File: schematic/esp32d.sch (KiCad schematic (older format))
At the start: 47 parts, among them IC1 CP2102N-A01-GQFN28R, J1 USB_B_Micro, J2 Conn_02x08_Odd_Even, J3 Conn_02x08_Odd_Even, J4 Conn_01x02, Q1 SS8050-G, Q2 SS8050-G, Q3 DMG2307L-7, SW1 SW_Push, U1 AMS1117-3.3, U2 ESP32-WROOM-32D, U3 DizzyBITLogo, U4 MCP73831-2-OT, U5 DizzyBIT-Layout

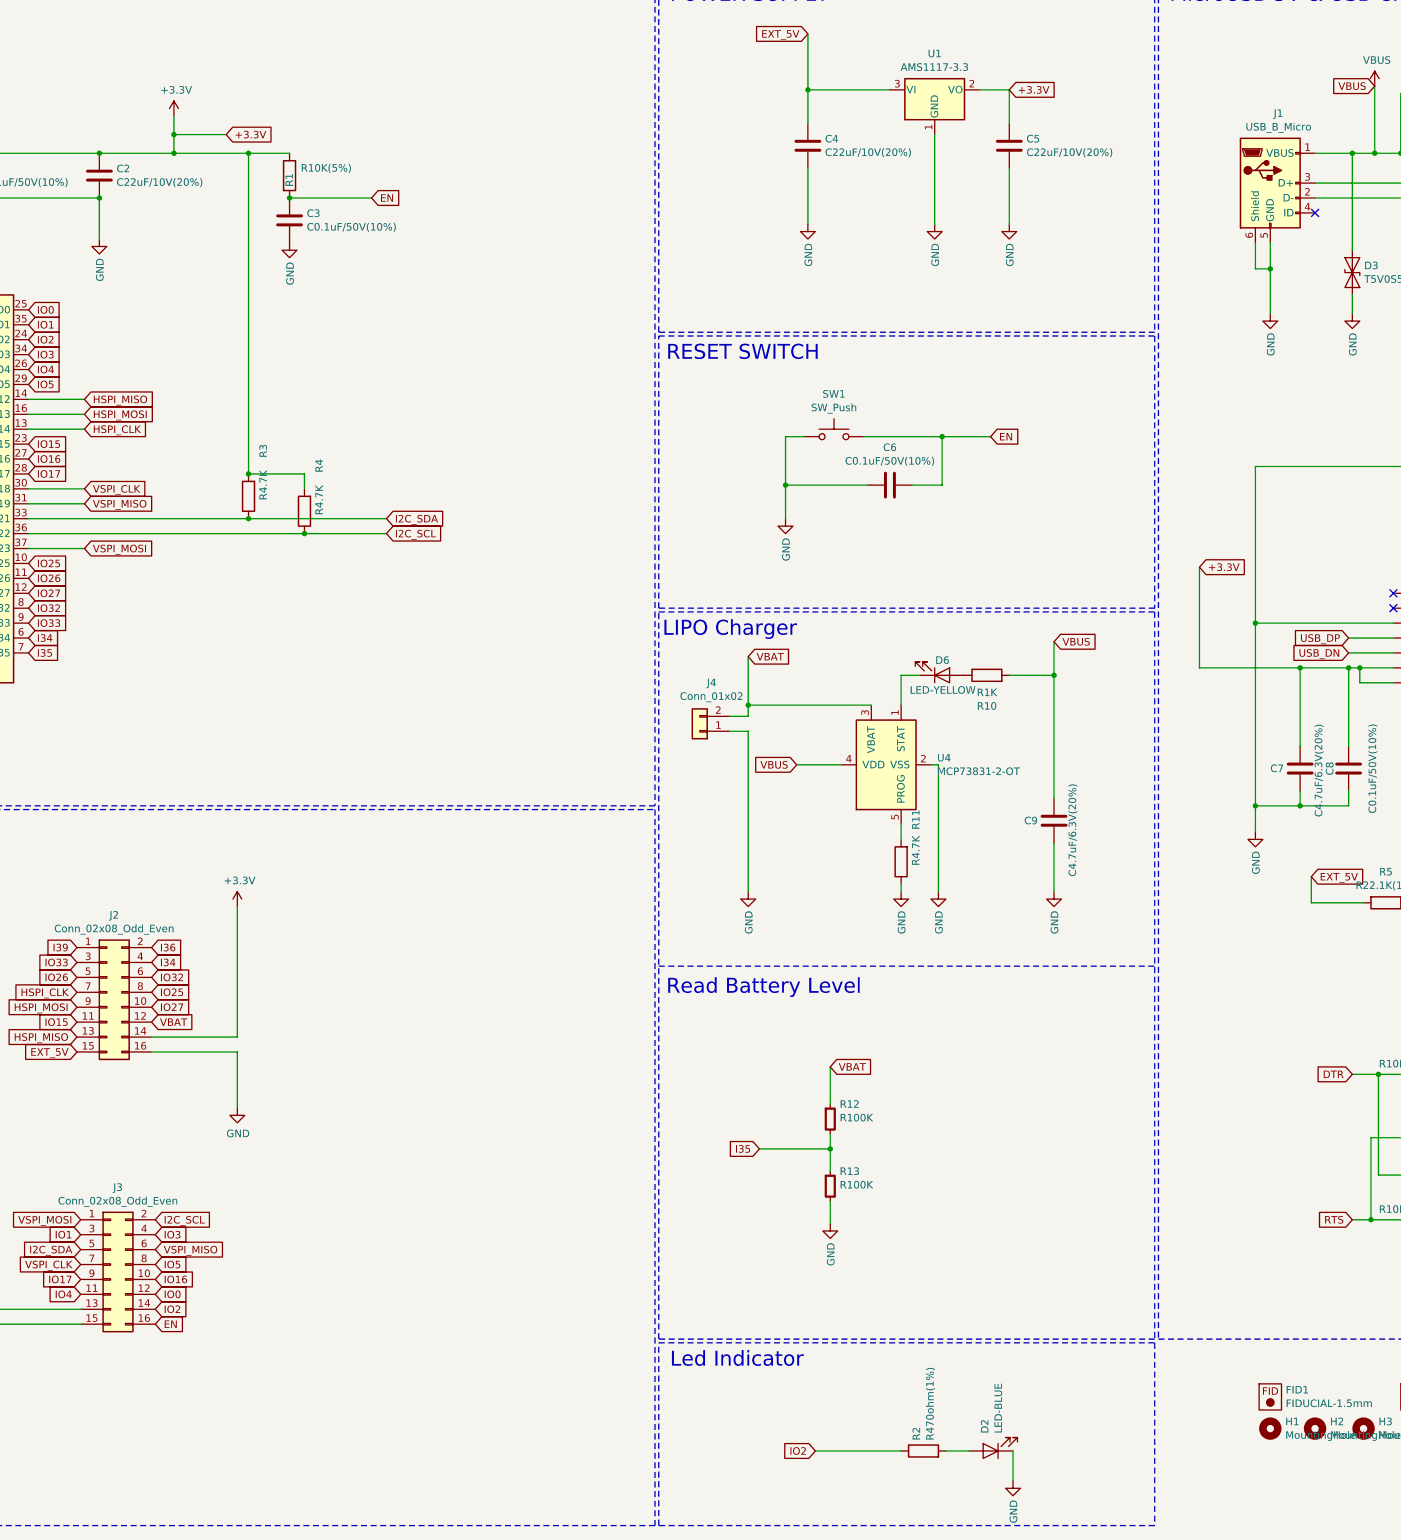
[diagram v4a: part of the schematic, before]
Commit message: Changed blue led PN for 3.3V
Added DIY project folder
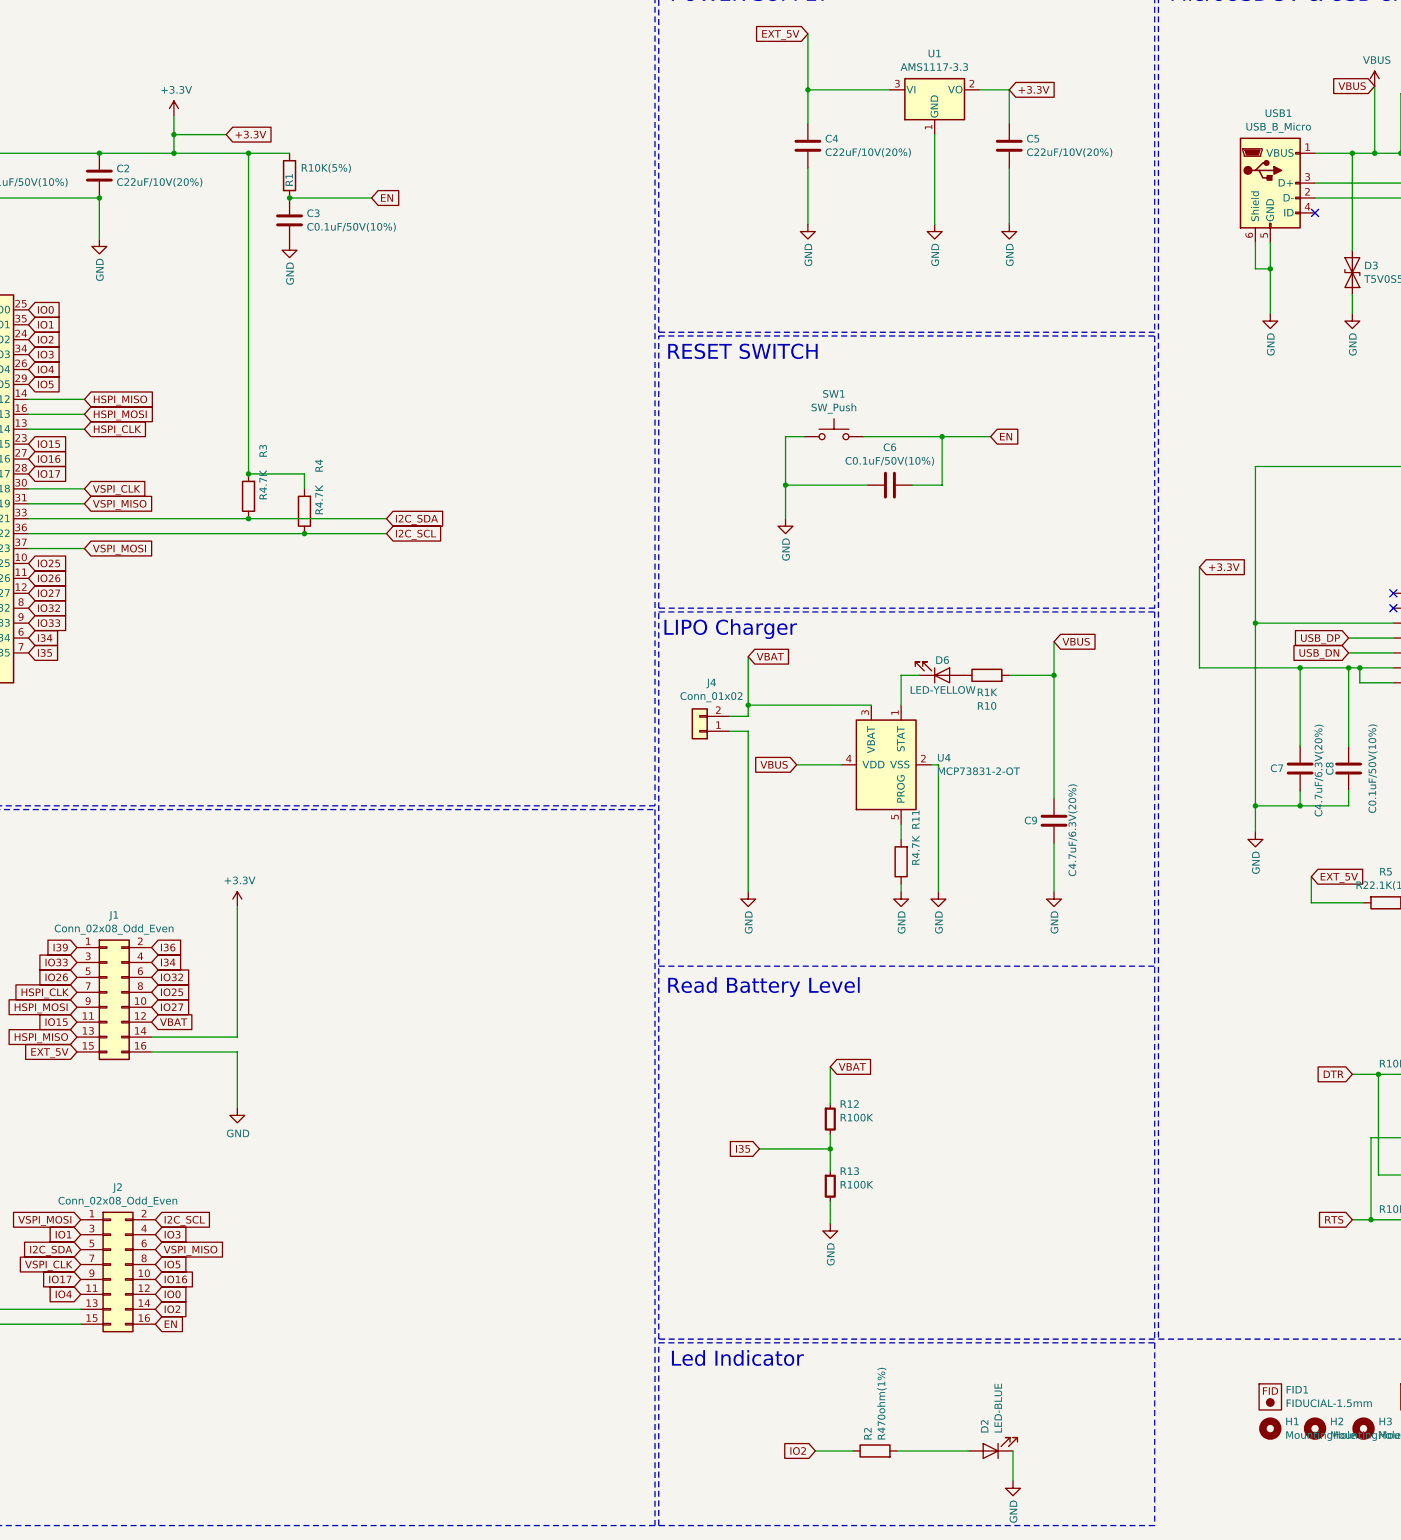
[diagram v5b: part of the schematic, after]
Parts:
- removed J2: Conn_02x08_Odd_Even, Connector_PinHeader_2.54mm:PinHeader_2x08_P2.54mm_Vertical, symbol Connector_Generic:Conn_02x08_Odd_Even
- added J1: Conn_02x08_Odd_Even, Connector_PinHeader_2.54mm:PinHeader_2x08_P2.54mm_Vertical, symbol Connector_Generic:Conn_02x08_Odd_Even
- D2: pn FC-A2012BK-470H2 -> 160-1579-2-ND
- renumbered J3 to J2, J1 to USB1
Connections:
- net +3V3: now also J1.14 (Pin_14)
- net EXT_5V: now also J1.15 (Pin_15)
- net GND: now also J1.16 (Pin_16)
- net HSPI_CLK: now also J1.7 (Pin_7)
- net HSPI_MISO: now also J1.13 (Pin_13)
- net HSPI_MOSI: now also J1.9 (Pin_9)
- net I34: now also J1.4 (Pin_4)
- net I36: now also J1.2 (Pin_2)
- net I39: now also J1.1 (Pin_1)
- net IO15: now also J1.11 (Pin_11)
- net IO25: now also J1.8 (Pin_8)
- net IO26: now also J1.5 (Pin_5)
- net IO27: now also J1.10 (Pin_10)
- net IO32: now also J1.6 (Pin_6)
- net IO33: now also J1.3 (Pin_3)
- net VBAT: now also J1.12 (Pin_12)
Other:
- moved on the sheet: R2
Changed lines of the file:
@@
 VSPI_MOSI
-$Comp
-L Connector_Generic:Conn_02x08_Odd_Even J2
-U 1 1 5D8B59AB
-P 4300 7475
-F 0 "J2" H 4350 7992 50  0000 C CNN
-F 1 "Conn_02x08_Odd_Even" H 4350 7901 50  0000 C CNN
-F 2 "Connector_PinHeader_2.54mm:PinHeader_2x08_P2.54mm_Vertical" H 4300 7475 50  0001 C CNN
-F 3 "http://www.connfly.com/userfiles/image/UpLoadFile/File/2014/11/24/PC104-003.pdf" H 4300 7475 50  0001 C CNN
-F 4 "PC104-003-2*8-B-1" H 4300 7475 50  0001 C CNN "pn"
-	1    4300 7475
-	1    0    0    -1
-$EndComp
 $Comp
 L power:+3.3V #PWR0101
@@
 L Device:R R2
 U 1 1 5C4E7D51
-P 9775 10550
-F 0 "R2" H 9845 10596 50  0000 L CNN
-F 1 "R470ohm(1%)" H 9845 10505 50  0000 L CNN
-F 2 "Resistor_SMD:R_0603_1608Metric" V 9705 10550 50  0001 C CNN
-F 3 "https://www.digikey.com/product-detail/en/yageo/RC0603FR-07470RL/311-470HRTR-ND/727256" H 9775 10550 50  0001 C CNN
-F 4 "311-470HRTR-ND" H 9775 10550 50  0001 C CNN "dk_pn"
-F 5 "RC0603FR-07470RL" H 9775 10550 50  0001 C CNN "pn"
-	1    9775 10550
+P 9450 10550
+F 0 "R2" H 9520 10596 50  0000 L CNN
+F 1 "R470ohm(1%)" H 9520 10505 50  0000 L CNN
+F 2 "Resistor_SMD:R_0603_1608Metric" V 9380 10550 50  0001 C CNN
+F 3 "https://www.digikey.com/product-detail/en/yageo/RC0603FR-07470RL/311-470HRTR-ND/727256" H 9450 10550 50  0001 C CNN
+F 4 "311-470HRTR-ND" H 9450 10550 50  0001 C CNN "dk_pn"
+F 5 "RC0603FR-07470RL" H 9450 10550 50  0001 C CNN "pn"
+	1    9450 10550
 	0    -1   -1   0
 $EndComp
 Wire Wire Line
-	9050 10550 9625 10550
+	9050 10550 9300 10550
 Connection ~ 9000 1425
 Text GLabel 9000 1050 0    50   Input ~ 0
@@
 F 1 "LED-BLUE" V 10172 10433 50  0000 R CNN
 F 2 "LED_SMD:LED_0805_2012Metric" H 10225 10550 50  0001 C CNN
-F 3 "" H 10225 10550 50  0001 C CNN
+F 3 "https://www.digikey.com/product-detail/en/lite-on-inc/LTST-C170TBKT/160-1579-2-ND/388527" H 10225 10550 50  0001 C CNN
 F 4 "FC-A2012BK-470H2 " V 10225 10550 50  0001 C CNN "dk_pn"
-F 5 "FC-A2012BK-470H2 " V 10225 10550 50  0001 C CNN "pn"
+F 5 "160-1579-2-ND" V 10225 10550 50  0001 C CNN "pn"
 	1    10225 10550
 	-1   0    0    1
 $EndComp
 Wire Wire Line
-	10075 10550 9925 10550
+	10075 10550 9600 10550
 $Comp
 L power:GND #PWR0110
@@
 	8000 4900 8000 3075
 $Comp
-L Connector:USB_B_Micro J1
+L Connector:USB_B_Micro USB1
 U 1 1 5C61F17B
 P 12100 2050
-F 0 "J1" H 12155 2517 50  0000 C CNN
+F 0 "USB1" H 12155 2517 50  0000 C CNN
 F 1 "USB_B_Micro" H 12155 2426 50  0000 C CNN
 F 2 "Connfly:DS1105-12" H 12250 2000 50  0001 C CNN
@@
 $EndComp
 $Comp
-L Connector_Generic:Conn_02x08_Odd_Even J3
+L Connector_Generic:Conn_02x08_Odd_Even J2
 U 1 1 5D8FF691
 P 4325 9300
-F 0 "J3" H 4375 9817 50  0000 C CNN
+F 0 "J2" H 4375 9817 50  0000 C CNN
 F 1 "Conn_02x08_Odd_Even" H 4375 9726 50  0000 C CNN
 F 2 "Connector_PinHeader_2.54mm:PinHeader_2x08_P2.54mm_Vertical" H 4325 9300 50  0001 C CNN
@@
 Wire Wire Line
 	3400 9600 3400 8725
+$Comp
+L Connector_Generic:Conn_02x08_Odd_Even J1
+U 1 1 5D9928C5
+P 4300 7475
+F 0 "J1" H 4350 7992 50  0000 C CNN
+F 1 "Conn_02x08_Odd_Even" H 4350 7901 50  0000 C CNN
+F 2 "Connector_PinHeader_2.54mm:PinHeader_2x08_P2.54mm_Vertical" H 4300 7475 50  0001 C CNN
+F 3 "http://www.connfly.com/userfiles/image/UpLoadFile/File/2014/11/24/PC104-003.pdf" H 4300 7475 50  0001 C CNN
+F 4 "PC104-003-2*8-B-1" H 4300 7475 50  0001 C CNN "pn"
+	1    4300 7475
+	1    0    0    -1
+$EndComp
 $EndSCHEMATC

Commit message: Finished the DIY board
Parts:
- removed Q3: DMG2307L-7, Package_TO_SOT_SMD:SOT-23, symbol SamacSys_Parts:DMG2307L-7
- added Q?: DMG2307L-7, SOT96P240X110-3N, symbol SamacSys_Parts:DMG2307L-7
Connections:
- net EXT_5V: now also Q?.2
- net VBAT: now also Q?.3
- net VBUS: now also Q?.1
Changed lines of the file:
@@
 	-1   0    0    1
 $EndComp
-Text GLabel 14375 1400 2    50   Input ~ 0
+Text GLabel 14375 1850 2    50   Input ~ 0
 EXT_5V
-Wire Wire Line
-	14375 1400 14375 1850
 Wire Wire Line
 	14375 1850 13775 1850
@@
 	1    0    0    -1
 $EndComp
-$Comp
-L SamacSys_Parts:DMG2307L-7 Q3
-U 1 1 5D8CC86D
-P 13475 1450
-F 0 "Q3" H 13904 1596 50  0000 L CNN
-F 1 "DMG2307L-7" H 13904 1505 50  0000 L CNN
-F 2 "Package_TO_SOT_SMD:SOT-23" H 13925 1400 50  0001 L CNN
-F 3 "https://componentsearchengine.com/Datasheets/1/DMG2307L-7.pdf" H 13925 1300 50  0001 L CNN
-F 4 "DMG2307L-7DITR-ND" H 13475 1450 50  0001 C CNN "dk_pn"
-F 5 "DMG2307L-7" H 13475 1450 50  0001 C CNN "pn"
-F 6 "https://www.digikey.com/product-detail/en/diodes-incorporated/DMG2307L-7/DMG2307L-7DITR-ND/2756043" H 13475 1450 50  0001 C CNN "dk_web"
-F 7 "P-Channel Enhancement MOSFET SOT-23 Diodes Inc DMG2307L-7 P-channel MOSFET Transistor, -2 A, -30 V, 3-Pin SOT23" H 13925 1200 50  0001 L CNN "Description"
-F 8 "1.1" H 13925 1100 50  0001 L CNN "Height"
-F 9 "621-DMG2307L-7" H 13925 1000 50  0001 L CNN "Mouser Part Number"
-F 10 "https://www.mouser.com/Search/Refine.aspx?Keyword=621-DMG2307L-7" H 13925 900 50  0001 L CNN "Mouser Price/Stock"
-F 11 "Diodes Inc." H 13925 800 50  0001 L CNN "Manufacturer_Name"
-F 12 "DMG2307L-7" H 13925 700 50  0001 L CNN "Manufacturer_Part_Number"
-	1    13475 1450
-	1    0    0    -1
-$EndComp
 Wire Wire Line
 	13475 1450 12975 1450
@@
 	1    0    0    -1
 $EndComp
+$Comp
+L SamacSys_Parts:DMG2307L-7 Q?
+U 1 1 5D999E77
+P 13475 1450
+F 0 "Q?" H 13904 1596 50  0000 L CNN
+F 1 "DMG2307L-7" H 13904 1505 50  0000 L CNN
+F 2 "SOT96P240X110-3N" H 13925 1400 50  0001 L CNN
+F 3 "https://componentsearchengine.com/Datasheets/1/DMG2307L-7.pdf" H 13925 1300 50  0001 L CNN
+F 4 "P-Channel Enhancement MOSFET SOT-23 Diodes Inc DMG2307L-7 P-channel MOSFET Transistor, -2 A, -30 V, 3-Pin SOT23" H 13925 1200 50  0001 L CNN "Description"
+F 5 "1.1" H 13925 1100 50  0001 L CNN "Height"
+F 6 "621-DMG2307L-7" H 13925 1000 50  0001 L CNN "Mouser Part Number"
+F 7 "https://www.mouser.com/Search/Refine.aspx?Keyword=621-DMG2307L-7" H 13925 900 50  0001 L CNN "Mouser Price/Stock"
+F 8 "Diodes Inc." H 13925 800 50  0001 L CNN "Manufacturer_Name"
+F 9 "DMG2307L-7" H 13925 700 50  0001 L CNN "Manufacturer_Part_Number"
+	1    13475 1450
+	1    0    0    -1
+$EndComp
